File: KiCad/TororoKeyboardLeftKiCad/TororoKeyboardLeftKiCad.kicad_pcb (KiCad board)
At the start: 2 copper layers, 139.7 x 99.2 mm, 97 parts, among them J1 MJ-4PP-9, SW1 SW_PUSH, SW10 SW_PUSH, SW11 SW_PUSH, SW12 SW_PUSH, SW13 SW_PUSH, SW14 SW_PUSH, SW15 SW_PUSH, SW16 SW_PUSH, SW17 SW_PUSH, SW18 SW_PUSH, SW19 SW_PUSH, SW2 SW_PUSH, SW20 SW_PUSH, SW21 SW_PUSH, SW22 SW_PUSH, SW23 SW_PUSH, SW24 SW_PUSH, SW25 SW_PUSH, SW26 SW_PUSH, SW27 SW_PUSH, SW28 SW_PUSH, SW29 SW_PUSH, SW3 SW_PUSH, SW4 SW_PUSH, SW5 SW_PUSH, SW6 SW_PUSH, SW7 SW_PUSH, SW8 SW_PUSH, SW9 SW_PUSH, U1 ProMicro

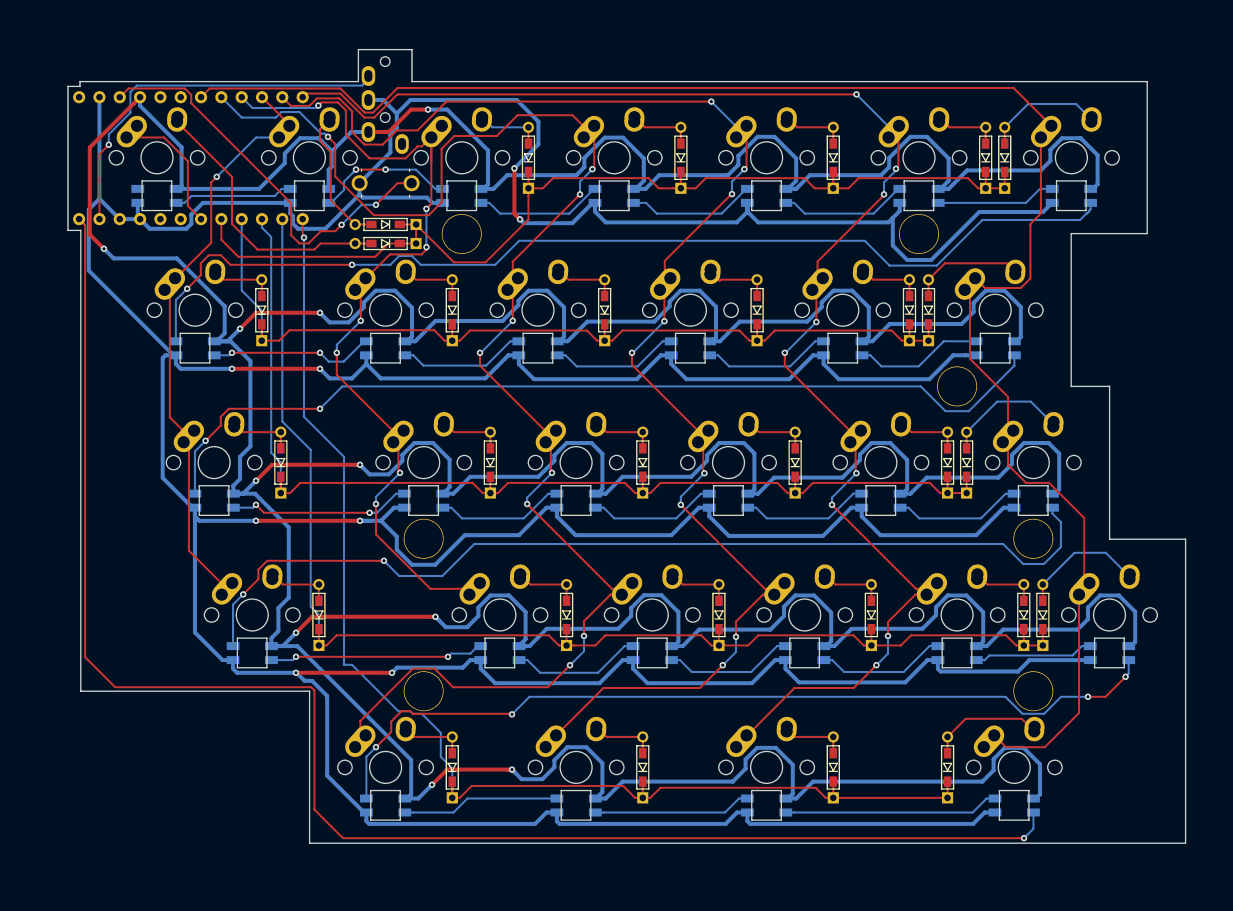
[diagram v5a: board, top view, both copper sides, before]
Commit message: GNDを塗りつぶし
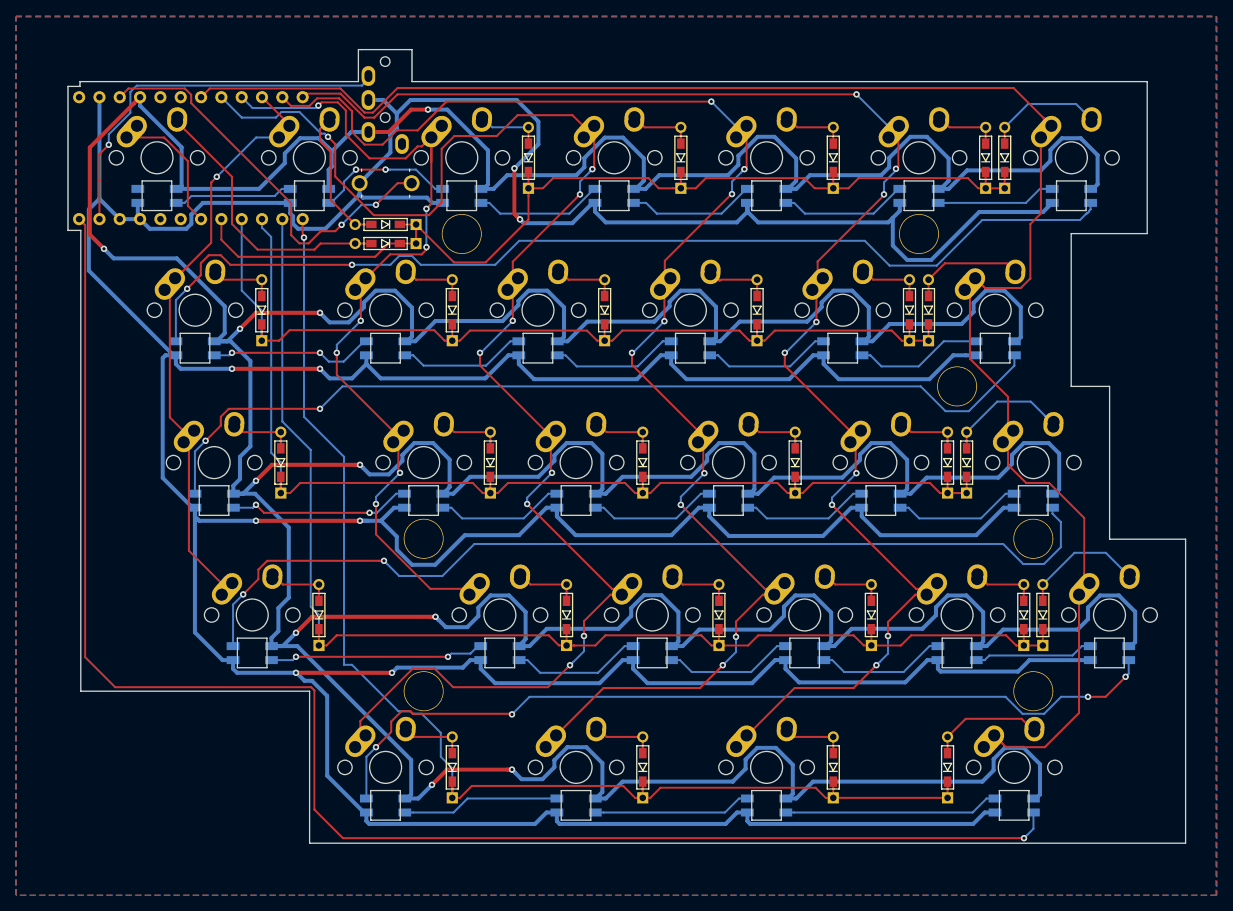
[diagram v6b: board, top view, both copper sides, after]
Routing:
- added copper zone on B.Cu, net GND
- added copper zone on F.Cu, net GND
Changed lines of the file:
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@@
   (segment (start 162.8775 117.0225) (end 158.6 121.3) (width 0.25) (layer F.Cu) (net 76))
   (segment (start 162.8775 102.235) (end 162.8775 117.0225) (width 0.25) (layer F.Cu) (net 76))
+  (zone (net 35) (net_name GND) (layer F.Cu) (hatch edge 0.508)
+    (connect_pads (clearance 0.508))
+    (min_thickness 0.254)
+    (fill yes (arc_segments 32) (thermal_gap 0.508) (thermal_bridge_width 0.508))
+    (polygon
+      (pts
+        (xy 180 139.8) (xy 30 139.8) (xy 30 29.9) (xy 180 29.9)
+      )
+    )
+  )
+  (zone (net 35) (net_name GND) (layer B.Cu) (hatch edge 0.508)
+    (connect_pads (clearance 0.508))
+    (min_thickness 0.254)
+    (fill yes (arc_segments 32) (thermal_gap 0.508) (thermal_bridge_width 0.508))
+    (polygon
+      (pts
+        (xy 180.1 139.8) (xy 30 139.8) (xy 30 30) (xy 180.1 30)
+      )
+    )
+  )
 )

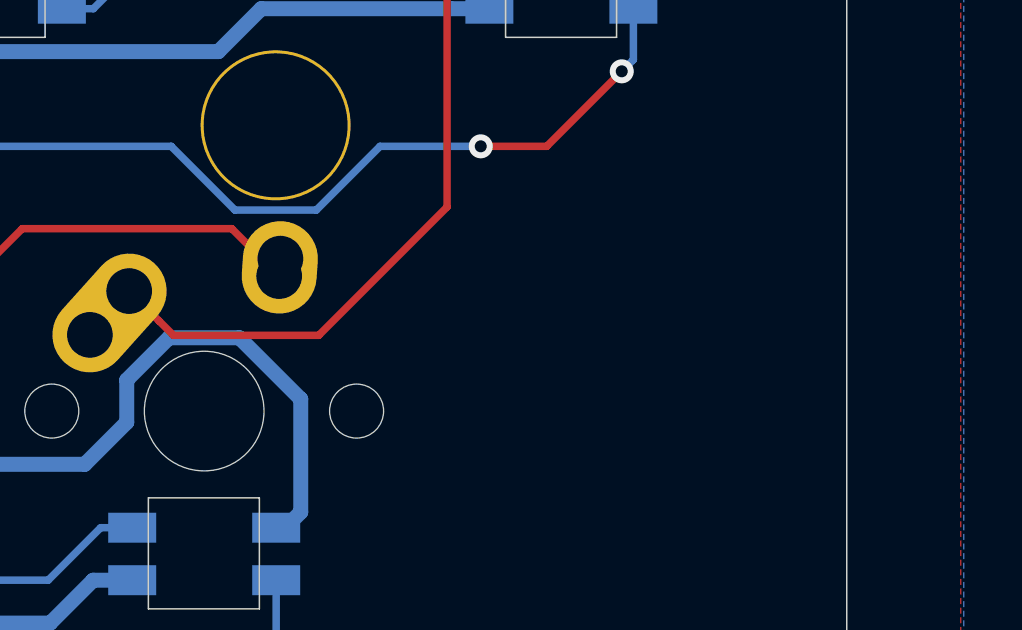
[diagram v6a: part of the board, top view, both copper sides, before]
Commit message: キーボード名とクレジットを配置
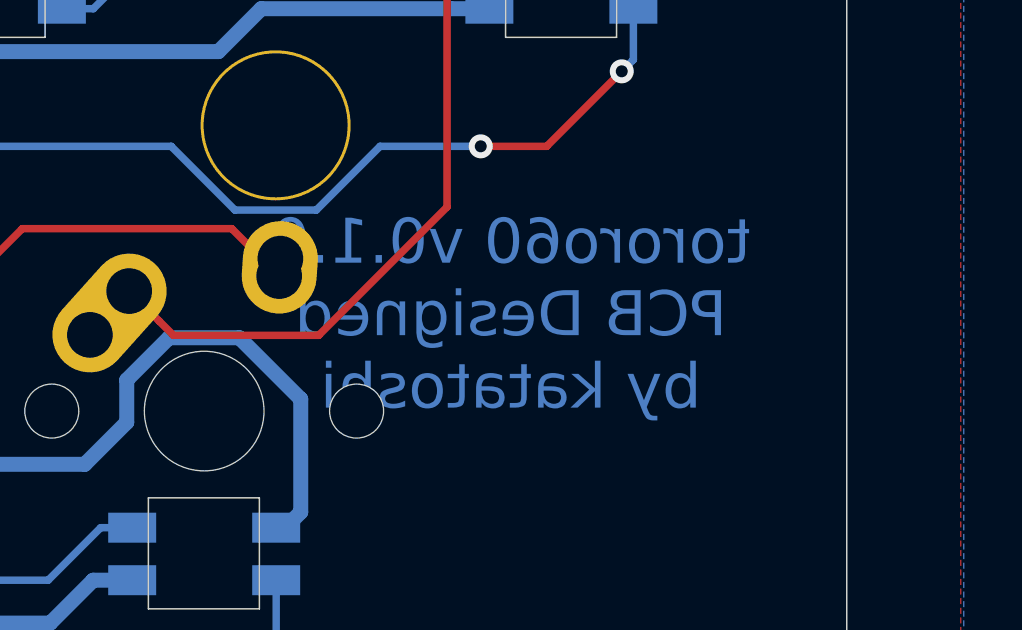
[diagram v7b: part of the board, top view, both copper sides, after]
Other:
- board text added: "tororo60 left v0.1.0 PCB Designed by katatoshi"
- board text added: "tororo60 v0.1.0 PCB Designed by katatoshi"
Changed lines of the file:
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@@
   (general
     (thickness 1.6)
-    (drawings 268)
+    (drawings 270)
     (tracks 1352)
     (zones 0)
@@
       (net 34 "Net-(D29-Pad2)"))
   )
+  (gr_text "tororo60 left v0.1.0\nPCB Designed by katatoshi" (at 43.5 95.3 90) (layer B.Mask)
+    (effects (font (size 1.5 1.5) (thickness 0.3)) (justify mirror))
+  )
+  (gr_text "tororo60 v0.1.0\nPCB Designed\nby katatoshi" (at 165 120.6) (layer B.Cu)
+    (effects (font (size 1.5 1.5) (thickness 0.3)) (justify mirror))
+  )
   (gr_line (start 38 38.7) (end 36.5 38.7) (layer Edge.Cuts) (width 0.05))

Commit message: 不要なテキストを除去
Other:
- board text removed: "tororo60 v0.1.0 PCB Designed by katatoshi"
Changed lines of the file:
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@@
   (general
     (thickness 1.6)
-    (drawings 270)
+    (drawings 269)
     (tracks 1352)
     (zones 0)
@@
     (visible_elements FFFFFF7F)
     (pcbplotparams
-      (layerselection 0x010fc_ffffffff)
+      (layerselection 0x010f0_ffffffff)
       (usegerberextensions false)
       (usegerberattributes false)
@@
       (outputformat 1)
       (mirror false)
-      (drillshape 1)
+      (drillshape 0)
       (scaleselection 1)
-      (outputdirectory ""))
+      (outputdirectory "gerber/"))
   )
   (net 0 "")
@@
     (effects (font (size 1.5 1.5) (thickness 0.3)) (justify mirror))
   )
-  (gr_text "tororo60 v0.1.0\nPCB Designed\nby katatoshi" (at 165 120.6) (layer B.Cu)
-    (effects (font (size 1.5 1.5) (thickness 0.3)) (justify mirror))
-  )
